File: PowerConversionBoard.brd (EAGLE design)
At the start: 72.4 x 71.1 mm, 46 parts, among them U1 LM2678, U2 LM2678

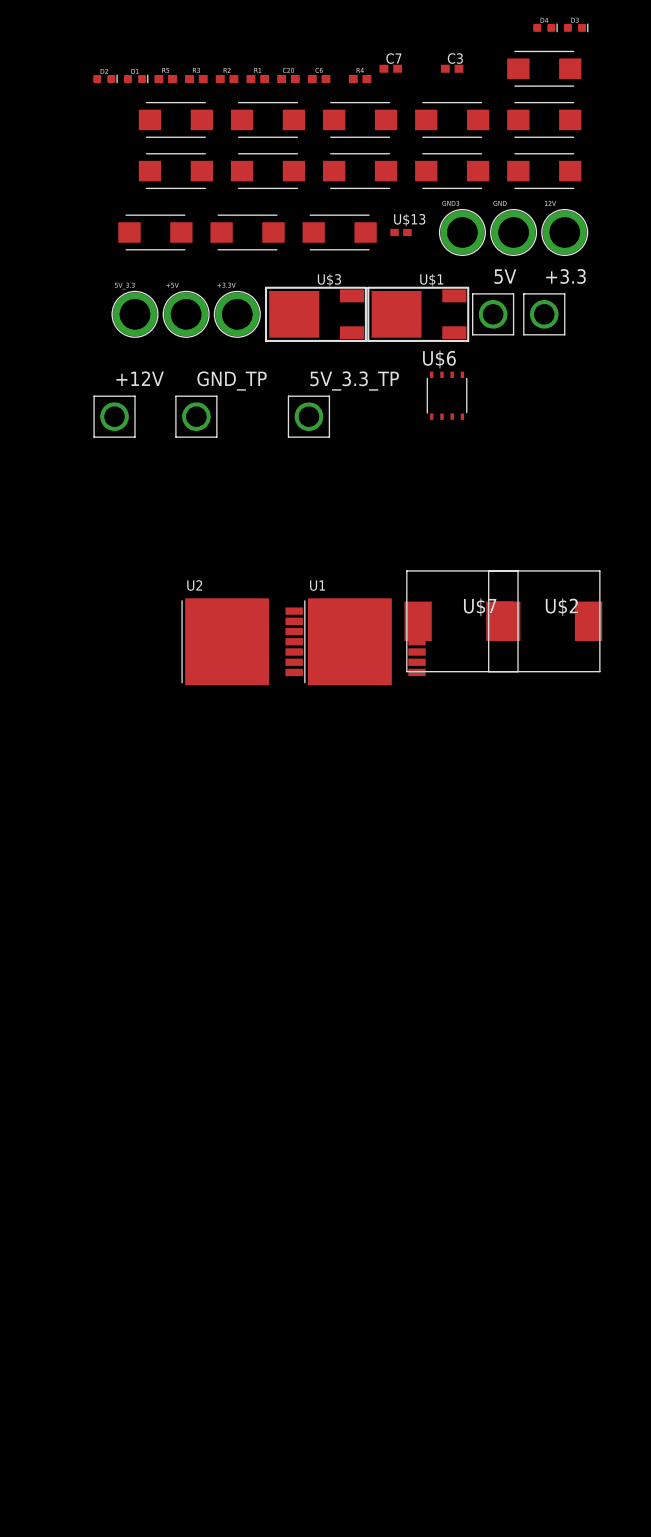
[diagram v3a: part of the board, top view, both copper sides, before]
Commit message: made progress on the buck controller supporting circuitry
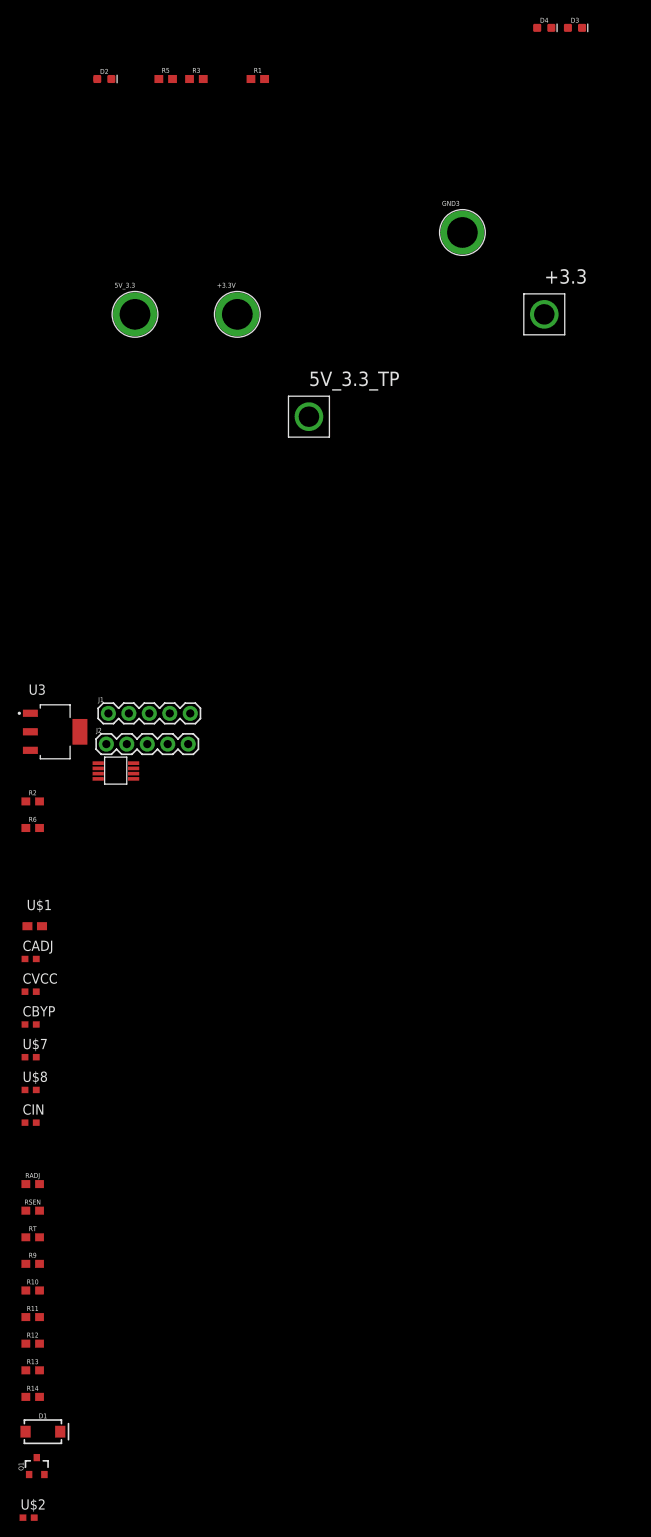
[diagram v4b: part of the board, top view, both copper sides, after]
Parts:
- removed +12V, 5V, GND_TP: TP, TP:TP
- removed +5V, 12V, GND: (no value), SparkFun-Connectors:BANANA_CONN
- removed C10, C11, C12, C24, C25, C26: 150uF, PowerComponents:CTAN(7.30_4.30MM)
- removed C14, C15, C16, C17, C18, C29, C30, C31: 10uF, PowerComponents:CTAN(7.30_4.30MM)
- removed C20, C6: 10nF, SparkFun-Capacitors:0603
- removed C3, C7: 0.47uF, rcl:C0603
- removed R4: 1.2 ohms, SparkFun-Resistors:0603
- removed U$13: 47 uF, Nordic_nRF:RESC0603_N
- removed U$3: SWITCHMODE_SCHOTTKY, PowerComponents:DPAK-3
- removed U$6: 5-33REGULATOR, 5-33Regulator:VOLTAGEREGULATOR
- removed U1, U2: LM2678, PowerComponents:LM2678
- added CADJ: 1000pF, Nordic_nRF:RESC0603_L
- added CBYP: 1uF, Nordic_nRF:RESC0603_L
- added CIN: 3.17uF, Nordic_nRF:RESC0603_L
- added CVCC: 0.47uF, Nordic_nRF:RESC0603_L
- added J1, J2: (no value), SparkFun-Connectors:1X05
- added Q1: 4.3A/20V/54mΩ, SparkFun-DiscreteSemi:SOT23-3
- added R10, R11, R12, R13, R14, R9: (no value), SparkFun-Resistors:0603
- added R6: 3.3k, SparkFun-Resistors:0603
- added RADJ: 1875, SparkFun-Resistors:0603
- added RSEN: 0.01, SparkFun-Resistors:0603
- added RT: 7.77k, SparkFun-Resistors:0603
- added U$4: LM5085, Buck_Controller:LM5085
- added U$8: (no value), Nordic_nRF:RESC0603_L
- added U3: AZ1117EH-3.3TRG1, Linear Regulator - AZ1117EH-3.3TRG1:SOT230P700X180-4N
- D1: value (none) -> 3A/40V/500mV; device SparkFun-LED:LED-0603 -> SparkFun-DiscreteSemi:SMA-DIODE
- R2: value 470 -> 10k
- R5: value 470 -> 5k
- U$1: value SWITCHMODE_SCHOTTKY -> (none); device PowerComponents:DPAK-3 -> Nordic_nRF:RESC0603_M
- U$2, U$7: value HCMA1305 -> (none); device Inductor_15uH - hcma1305:HCMA1305 -> Nordic_nRF:RESC0603_L
- moved D1 168.3 mm to (-81.3, -91.7)
- moved U$2 128.4 mm to (-83.1, -102.4)
- moved R2 92.9 mm to (-82.5, -13.5)
- moved U$1 89.8 mm to (-82.3, -29.0)
- moved U$7 76.2 mm to (-82.8, -45.2)
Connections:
- removed net +5V: +5V.P$1, 5V.P$1, C10.+, C11.+, C12.+, R2.2, U$2.P$2
- removed net N$11: C15.+, C16.+, C17.+, C18.+, C7.1, U1.2
- removed net N$14: C6.1, U1.3
- new net FB: R12.1, R13.2, U$4.3, U$7.2
- new net ISEN: Q1.2, RSEN.2, U$4.5
- new net N$3: CVCC.1, U$4.7
- new net N$9: R14.2, U$7.1, U$8.2
- new net PGATE: Q1.1, U$4.6
- net +3.3V: now also J2.5, U3.2, U3.4; no longer U$13.1, U$6.1, U$6.2
- net +48V: now also CBYP.1, CIN.1, CVCC.2, J1.5, RT.1, U$4.8; no longer +12V.P$1, 12V.P$1, C14.+, C29.+, C3.1, C30.+, C31.+, U2.2
- net +5V_3.3V: now also J2.1, J2.2, J2.3, J2.4, U3.3; no longer C24.+, C25.+, C26.+, U$6.5, U$6.8, U$7.P$2, U2.6
- net GND: now also CBYP.2, CIN.2, D1.A, J1.1, J1.2, J1.3, J1.4, R12.2, U$4.4, U3.1; no longer C10.-, C11.-, C12.-, C14.-, C15.-, C16.-, C17.-, C18.-, C24.-, C25.-, C26.-, C29.-, C3.2, C30.-, C31.-, C7.2, D1.C, GND.P$1, GND_TP.P$1, R4.1, U$1.P$1, U$1.P$3, U$3.P$1, U$3.P$3, U$6.3, U1.4, U1.TAB, U2.4, U2.TAB
- net N$1: now also CADJ.1, RADJ.1, U$4.1; no longer C6.2, U$1.P$4, U$2.P$1, U1.1, U1.6
- net N$10: now also R13.1, U$1.2, U$8.1; no longer R4.2, U$13.2
- net N$2: now also CADJ.2, RADJ.2, RSEN.1; no longer C20.1, U2.3
- net N$7: now also D1.C, Q1.3, R14.1, U$1.1; no longer C20.2, U$3.P$4, U$7.P$1, U2.1
- net N$8: now also RT.2, U$4.2; no longer D1.A, R2.1

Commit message: threw the pieces onto the board in no particular order and finsihed the skeleton of the circuit around the buck controller. Still need to get the standard values for the inductors and capacitors, but finished the resistors. Also need to figure oit the MOSFET and Schottky diode
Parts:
- removed R1: 470, SparkFun-Resistors:0603
- removed R10, R11, R12, R13, R14, R9: (no value), SparkFun-Resistors:0603
- removed R2: 10k, SparkFun-Resistors:0603
- removed R5: 5k, SparkFun-Resistors:0603
- removed R6: 3.3k, SparkFun-Resistors:0603
- removed U$2, U$7, U$8: (no value), Nordic_nRF:RESC0603_L
- removed U$4: LM5085, Buck_Controller:LM5085
- added 1R, 3R: 470, SparkFun-Resistors:0603
- added 5R: 5k, SparkFun-Resistors:0603
- added C1: 3300pF, Nordic_nRF:RESC0201_M
- added C2: 0.1uF, Nordic_nRF:RESC0201_M
- added COUPLE: 1nF, SparkFun-Capacitors:0603
- added COUT: 100uF, Nordic_nRF:RESC0201_M
- added L1: 12.4uH, Nordic_nRF:RESC0201_M
- added RFB1: 3.3k, SparkFun-Resistors:0603
- added RFB2: 10k, SparkFun-Resistors:0603
- CADJ, CBYP, CIN, CVCC: device Nordic_nRF:RESC0603_L -> Nordic_nRF:RESC0201_M
- Q1: value 4.3A/20V/54mΩ -> 6.5A/20V/35mΩ; device SparkFun-DiscreteSemi:SOT23-3 -> SparkFun-DiscreteSemi:SO08
- R3: value 470 -> 9.1k
- RADJ: value 1875 -> 1.8k
- RT: value 7.77k -> 77.7k
- U$1: value (none) -> LM5085; device Nordic_nRF:RESC0603_M -> Buck_Controller:LM5085
- moved Q1 178.2 mm to (30.2, 42.4), turned to 90 degrees
- moved D2 155.9 mm to (69.3, 14.2), turned to 90 degrees
- moved CIN 153.4 mm to (41.1, 37.1)
- moved RT 150.2 mm to (30.7, 31.0)
- moved CVCC 146.6 mm to (41.1, 41.1)
- moved D1 144.8 mm to (13.0, 18.3)
- moved CBYP 144.4 mm to (41.1, 33.0)
- moved RADJ 141.8 mm to (30.7, 24.4)
- moved RSEN 139.9 mm to (30.7, 17.8)
- moved CADJ 138.6 mm to (41.1, 29.0)
- moved U$1 133.4 mm to (22.9, 53.1)
- moved D4 116.7 mm to (69.3, 6.35), turned to 90 degrees
- moved 5V_3.3_TP 116.5 mm to (67.8, 44.2)
- moved R3 111.6 mm to (30.7, 14.5)
- moved D3 111.3 mm to (69.3, 10.2), turned to 90 degrees
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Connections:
- removed net +5V_3.3V: 5V_3.3.P$1, 5V_3.3_TP.P$1, J2.1, J2.2, J2.3, J2.4, R1.2, U3.3
- removed net FB: R12.1, R13.2, U$4.3, U$7.2
- removed net ISEN: Q1.2, RSEN.2, U$4.5
- removed net N$1: CADJ.1, RADJ.1, U$4.1
- removed net N$8 (its old number): RT.2, U$4.2
- removed net PGATE: Q1.1, U$4.6
- new net +5V: 1R.2, 5V_3.3.P$1, 5V_3.3_TP.P$1, C1.1, COUPLE.1, COUT.1, J2.1, J2.2, J2.3, J2.4, L1.2, RFB2.1, U3.3
- new net N$11: C1.2, C2.1, R3.2
- new net N$14: C2.2, RFB1.1, RFB2.2, U$1.3
- new net N$2: CADJ.1, RADJ.1, U$1.1
- net +3.3V: now also 3R.2; no longer R3.2
- net +48V: now also 5R.2, CVCC.1, RT.2, U$1.2, U$1.8; no longer CVCC.2, R5.2, U$4.8
- net GND: now also COUPLE.2, COUT.2, RFB1.2, U$1.4; no longer R12.2, U$4.4
- net N$10: now also D1.C, L1.1, Q1.5, Q1.6, Q1.7, Q1.8, R3.1; no longer R13.1, U$1.2, U$8.1
- net N$3: now also CVCC.2, U$1.7; no longer CVCC.1, U$4.7
- net N$4: now also 5R.1; no longer R5.1
- net N$5: now also 3R.1; no longer R3.1
- net N$6: now also 1R.1; no longer R1.1
- net N$7: now also Q1.4, U$1.6; no longer D1.C, Q1.3, R14.1, U$1.1
- net N$9: now also Q1.1, Q1.2, Q1.3, RSEN.2, U$1.5; no longer R14.2, U$7.1, U$8.2

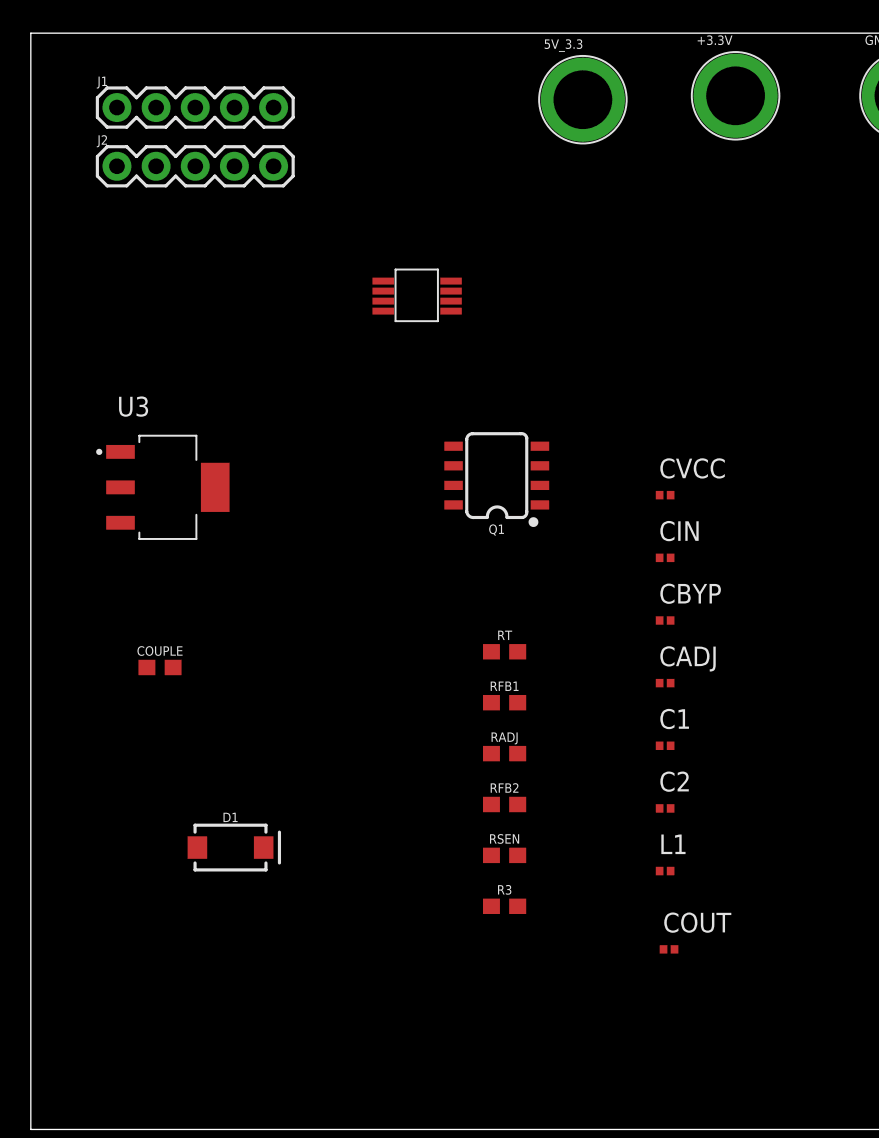
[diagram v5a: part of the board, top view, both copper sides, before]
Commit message: Changed Buck Controller output to 5.2V (did not change net label); added RC Circuit to Linear regulator; added connection to distribution board
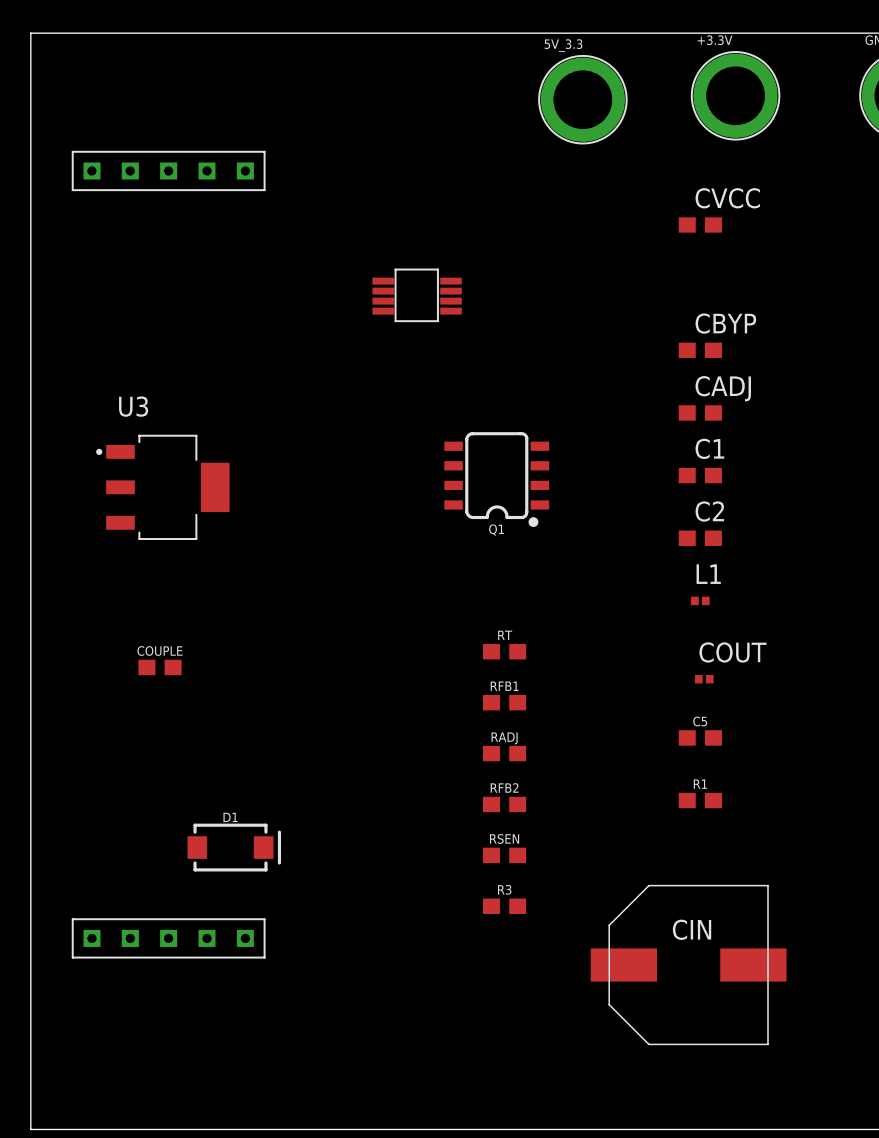
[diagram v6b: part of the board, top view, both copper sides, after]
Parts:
- removed J1, J2: (no value), SparkFun-Connectors:1X05
- added C5: 47uF, SparkFun-Capacitors:0603
- added R1: 1.2 Ohms, SparkFun-Resistors:0603
- added U$2: DIST_TO_CONV, Dist_To_Conv_Connector:DIST_TO_CONV
- C1, C2, CADJ, CBYP, CVCC: device Nordic_nRF:RESC0201_M -> SparkFun-Capacitors:0603
- CIN: value 3.17uF -> 3.33uF; device Nordic_nRF:RESC0201_M -> brick-capacitor-UCM1H331MNL1GS:CAPAE1030X1050N
- L1: value 12.4uH -> 13uH
- R3: value 9.1k -> 8.6k
- RADJ: value 1.8k -> 9.5k
- RFB1: value 3.3k -> 4.7k
- RFB2: value 10k -> 15k
- RSEN: value 0.01 -> 0.05
- RT: value 77.7k -> 82k
- moved CIN 26.5 mm to (42.7, 10.7)
- moved COUT 17.7 mm to (43.7, 29.2)
- moved C1 17.7 mm to (43.4, 42.4)
- moved C2 17.7 mm to (43.4, 38.4)
- moved CADJ 17.7 mm to (43.4, 46.5)
- moved L1 17.7 mm to (43.4, 34.3)
- moved CBYP 17.7 mm to (43.4, 50.5)
- moved CVCC 17.7 mm to (43.4, 58.7)
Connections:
- new net N$1: RT.1, U$1.2
- new net N$12: C5.2, R1.2
- net +3.3V: now also C5.1, U$2.3V, U$2.48V; no longer J2.5
- net +48V: now also CIN.+; no longer CIN.1, J1.5, RT.1, U$1.2
- net +5V: now also U$2.5V_1, U$2.5V_2, U$2.5V_3, U$2.5V_4; no longer J2.1, J2.2, J2.3, J2.4
- net GND: now also CIN.-, R1.1, U$2.GND_1, U$2.GND_2, U$2.GND_3, U$2.GND_4; no longer CIN.2, J1.1, J1.2, J1.3, J1.4

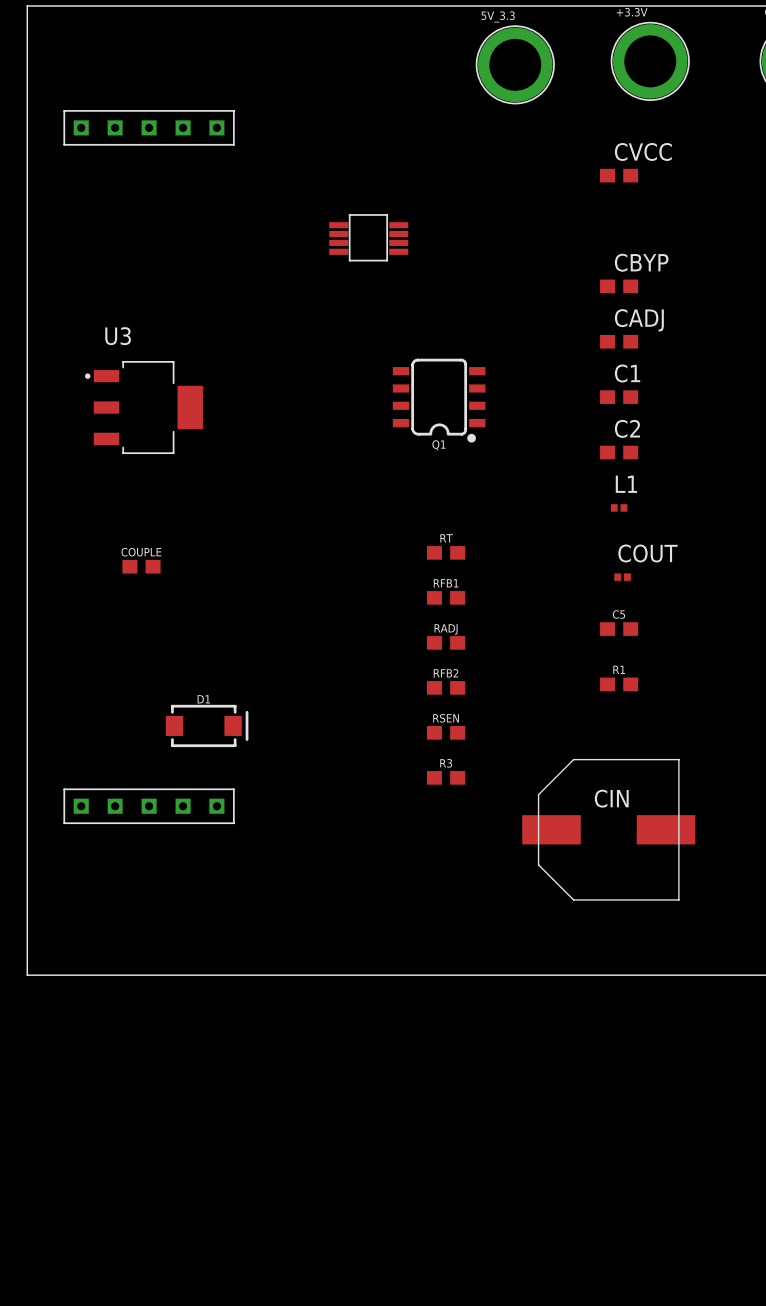
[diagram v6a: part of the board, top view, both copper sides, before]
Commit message: Copied in last year's capacitor and inductor
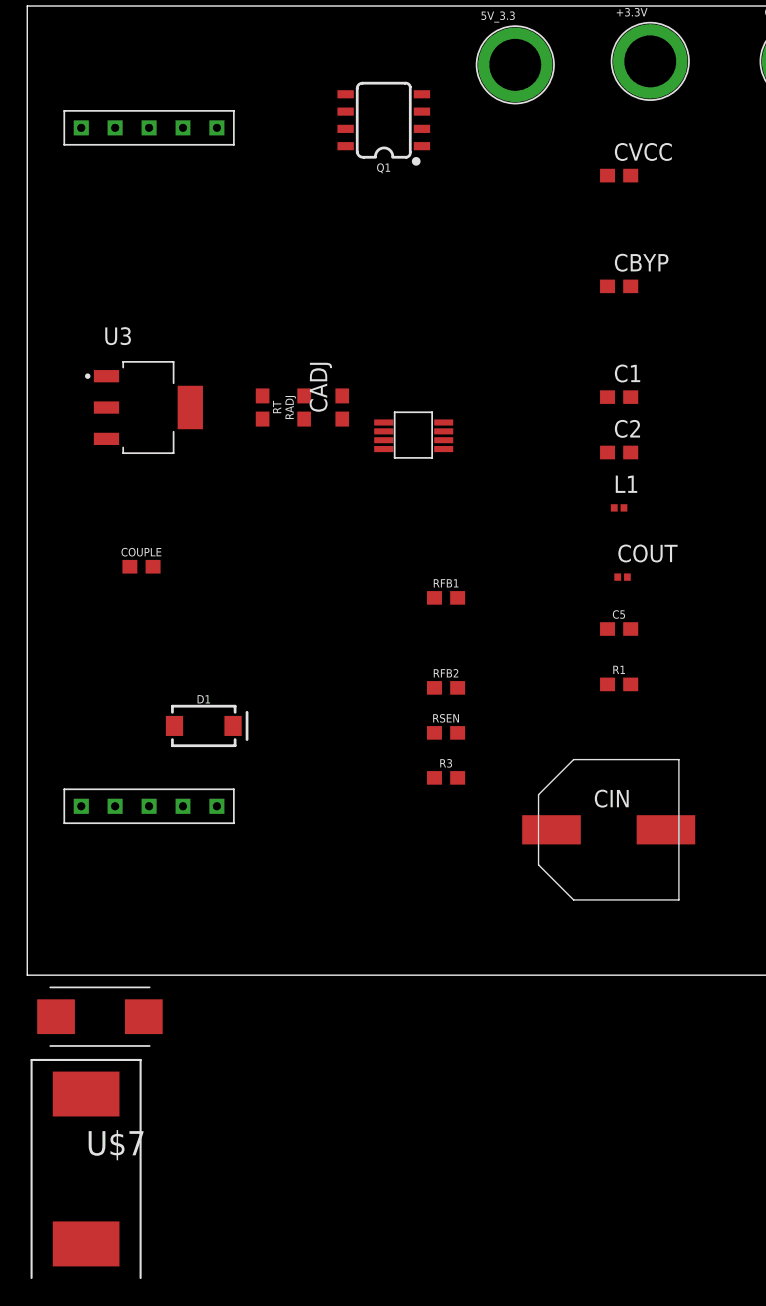
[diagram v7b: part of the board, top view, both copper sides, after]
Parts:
- added C24: 150uF, PowerComponents:CTAN(7.30_4.30MM)
- added U$7: HCM1305, HCM1305:HCM1305
- D1: value 3A/40V/500mV -> (none)
- Q1: value 6.5A/20V/35mΩ -> (none)
- moved CADJ 20.9 mm to (23.1, 41.7), turned to 90 degrees
- moved Q1 20.7 mm to (26.2, 62.7)
- moved RADJ 20.2 mm to (20.3, 41.7), turned to 90 degrees
- moved RT 17.2 mm to (17.3, 41.7), turned to 270 degrees
- moved U$1 14.8 mm to (26.2, 38.6)
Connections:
- removed net N$1: RT.1, U$1.2
- net +48V: now also RT.1, U$1.2

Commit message: copied old parts over
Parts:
- removed COUT: 100uF, Nordic_nRF:RESC0201_M
- removed D1: (no value), SparkFun-DiscreteSemi:SMA-DIODE
- removed L1: 13uH, Nordic_nRF:RESC0201_M
- added U$4: SWITCHMODE_SCHOTTKY, PowerComponents:DPAK-3
- CIN: value 3.33uF -> 47uF
- RSEN: value 0.05 -> 0.01; device SparkFun-Resistors:0603 -> INA4181A4:CSS2H-2512
- moved RSEN 64.9 mm to (3.05, -40.9)
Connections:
- removed net N$8: CADJ.2, RADJ.2, RSEN.1
- net +48V: now also CADJ.2, RADJ.2, RSEN.2
- net +5V: now also C24.+, U$7.2; no longer COUT.1, L1.2
- net GND: now also C24.-, U$4.P$1, U$4.P$3; no longer COUT.2, D1.A
- net N$10: now also U$4.P$4, U$7.1; no longer D1.C, L1.1
- net N$9: now also RSEN.1; no longer RSEN.2
